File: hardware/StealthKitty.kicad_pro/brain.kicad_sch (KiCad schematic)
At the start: 16 parts, among them J4 M50-3600742, J5 Conn_ST_STDC14, SW1 SW_Push, SW2 SW_Push, U1 STM32G431CBUx, Y1 Crystal_GND24_Small

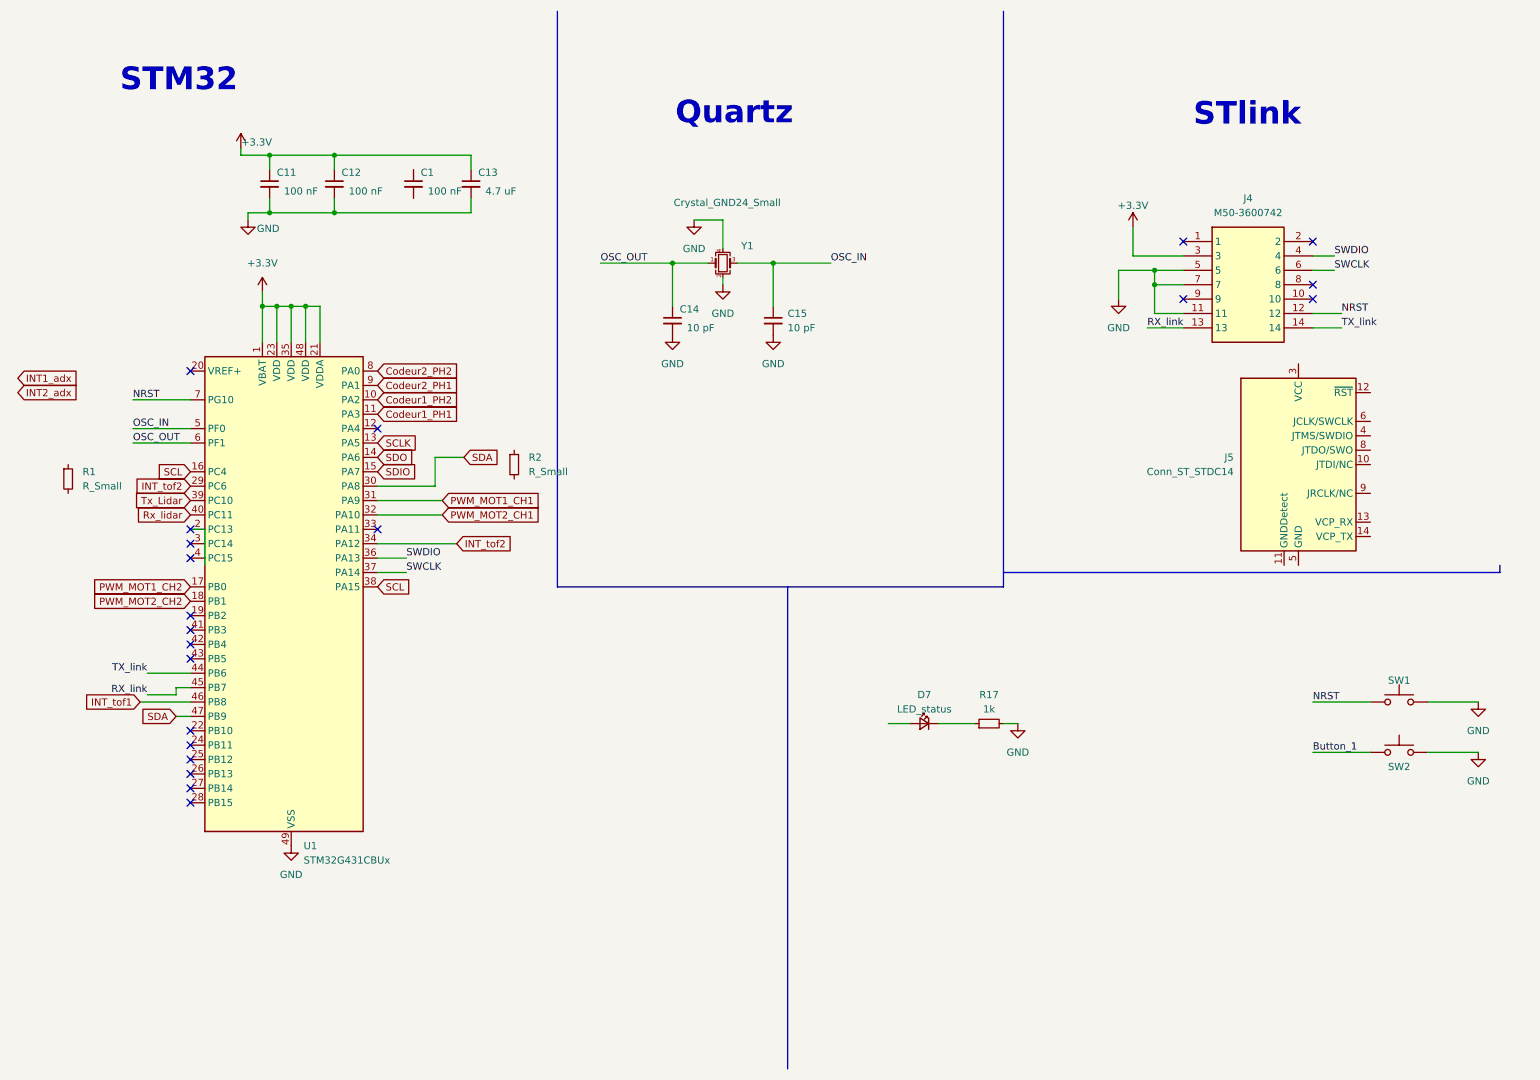
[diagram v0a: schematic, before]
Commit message: réassignation pins stm32, ajout des modifs de la partie power, ajout des modfis de la revue de projet 02/10/24, modifs du 3/10/24 voir readme
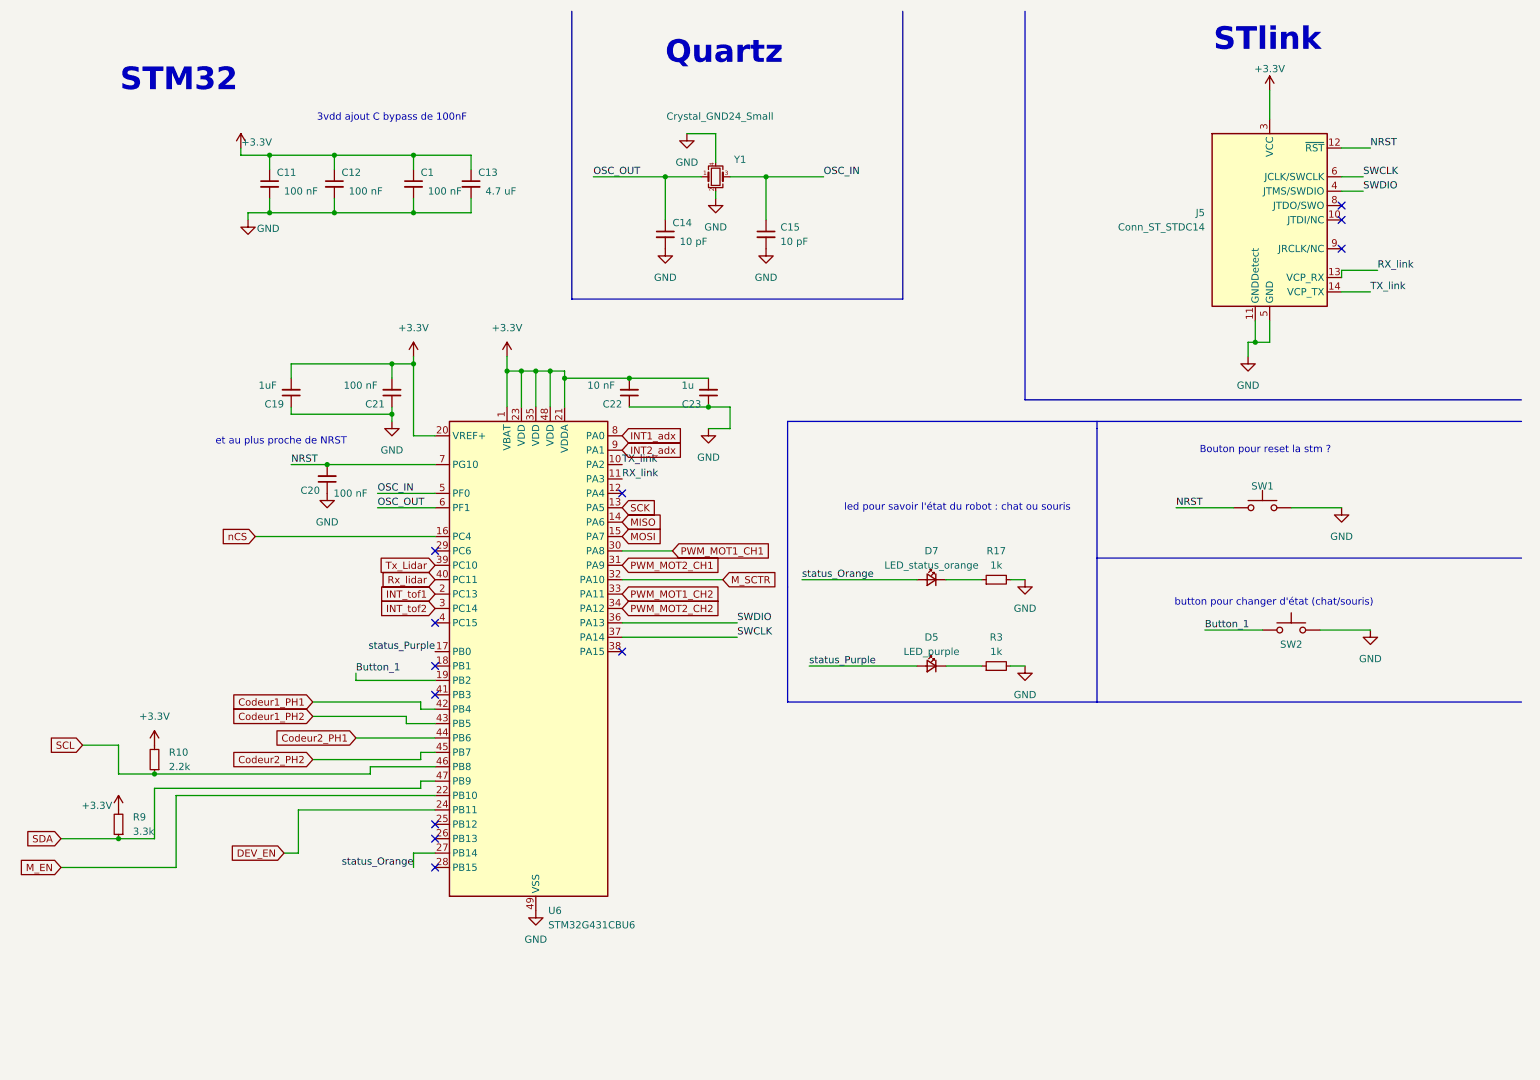
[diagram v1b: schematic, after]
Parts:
- removed J4: M50-3600742, Crystal:Crystal_SMD_3225-4Pin_3.2x2.5mm, symbol M50-3600742:M50-3600742
- removed R1, R2: R_Small, symbol Device:R_Small
- removed U1: STM32G431CBUx, Package_DFN_QFN:QFN-48-1EP_7x7mm_P0.5mm_EP5.6x5.6mm, symbol MCU_ST_STM32G4:STM32G431CBUx
- added C19: 1uF, symbol Device:C_Small
- added C20, C21: 100 nF, symbol Device:C_Small
- added C22: 10 nF, symbol Device:C_Small
- added C23: 1u, symbol Device:C_Small
- added D5: LED_purple, LED_SMD:LED_0603_1608Metric_Pad1.05x0.95mm_HandSolder, symbol Device:LED_Small
- added R10: 2.2k, symbol Device:R_Small
- added R3: 1k, Resistor_SMD:R_0603_1608Metric_Pad0.98x0.95mm_HandSolder, symbol Device:R_Small
- added R9: 3.3k, symbol Device:R_Small
- added U6: STM32G431CBU6, Package_DFN_QFN:QFN-48-1EP_7x7mm_P0.5mm_EP5.6x5.6mm, symbol MCU_ST_STM32G4:STM32G431CBUx
- D7: value LED_status -> LED_status_orange
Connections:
- net +3.3V: now also C1.1, J5.3 (VCC), C19.2, C21.2, C22.2, C23.2, R10.2, R9.2, U6.1 (VBAT), U6.20 (VREF+), U6.21 (VDDA), U6.23 (VDD), U6.35 (VDD), U6.48 (VDD)
- net Button_1: now also U6.19 (PB2)
- net Codeur1_PH1: now also U6.42 (PB4)
- net Codeur1_PH2: now also U6.43 (PB5)
- net Codeur2_PH1: now also U6.44 (PB6)
- net Codeur2_PH2: now also U6.45 (PB7)
- net GND: now also C1.2, J5.11 (GNDDetect), J5.5 (GND), J5.7 (GND), C19.1, C20.1, C21.1, C22.1, C23.1, R3.2, U6.49 (VSS)
- net INT1_adx: now also U6.8 (PA0)
- net INT2_adx: now also U6.9 (PA1)
- net INT_tof1: now also U6.2 (PC13)
- net INT_tof2: now also U6.3 (PC14)
- net NRST: now also J5.12 (~{RST}), C20.2, U6.7 (PG10)
- net OSC_IN: now also U6.5 (PF0)
- net OSC_OUT: now also U6.6 (PF1)
- net PWM_MOT1_CH1: now also U6.30 (PA8)
- net PWM_MOT1_CH2: now also U6.33 (PA11)
- net PWM_MOT2_CH1: now also U6.31 (PA9)
- net PWM_MOT2_CH2: now also U6.34 (PA12)
- net RX_link: now also J5.13 (VCP_RX), U6.11 (PA3)
- net Rx_lidar: now also U6.40 (PC11)
- net SCL: now also R10.1, U6.46 (PB8)
- net SDA: now also R9.1, U6.47 (PB9)
- net SWCLK: now also J5.6 (JCLK/SWCLK), U6.37 (PA14)
- net SWDIO: now also J5.4 (JTMS/SWDIO), U6.36 (PA13)
- net TX_link: now also J5.14 (VCP_TX), U6.10 (PA2)
- net Tx_Lidar: now also U6.39 (PC10)
- net status_Orange: now reaches D7.2 (A)
- net status_Orange: now also U6.27 (PB14)
- new net: D5.1 (K), R3.1
- new net DEV_EN: U6.24 (PB11)
- new net MISO: U6.14 (PA6)
- new net MOSI: U6.15 (PA7)
- new net M_EN: U6.22 (PB10)
- new net M_SCTR: U6.32 (PA10)
- new net SCK: U6.13 (PA5)
- new net nCS: U6.16 (PC4)
- new net status_Purple: D5.2 (A), U6.17 (PB0)
- no-connect marks 21 -> 12
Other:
- note added: "3vdd ajout C bypass de 100nF"
- note added: "Bouton pour reset la stm ?"
- note added: "button pour changer d'état (chat/souris)"
- note added: "et au plus proche de NRST"
- note added: "led pour savoir l'état du robot : chat ou souris"
- moved on the sheet: C14, C15, D7, J5, R17, SW1, SW2, Y1

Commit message: MAJ routage equipe
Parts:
- added H401, H402, H403, H404: ~, MountingHole:MountingHole_3.2mm_M3_Pad_Via, symbol Mechanical:MountingHole_Pad
- C1, C11, C12, C14, C15, C20, C21, C22: footprint (none) -> Capacitor_SMD:C_0402_1005Metric_Pad0.74x0.62mm_HandSolder
- C13, C19, C23: footprint (none) -> Capacitor_SMD:C_0603_1608Metric_Pad1.08x0.95mm_HandSolder
- R10, R9: footprint (none) -> Resistor_SMD:R_0603_1608Metric_Pad0.98x0.95mm_HandSolder
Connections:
- net GND: now also H401.1, H402.1, H403.1, H404.1

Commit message: Confirmation placement equipe
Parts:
- renumbered C11 to C401, C19 to C402, C20 to C403, C12 to C404, C21 to C405, C1 to C406, C13 to C407, C22 to C408, C14 to C409, C23 to C410, C15 to C411, D7 to D401, D5 to D402, J5 to J401, R9 to R401, R10 to R402, R17 to R403, R3 to R404, SW1 to SW401, SW2 to SW402, U6 to U401, Y1 to Y401

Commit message: Dernier Modif 08/10/2024
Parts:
- C401, C403, C404, C405, C406, C408, C409, C411: footprint Capacitor_SMD:C_0402_1005Metric_Pad0.74x0.62mm_HandSolder -> Capacitor_SMD:C_0402_1005Metric
- C402, C407, C410: footprint Capacitor_SMD:C_0603_1608Metric_Pad1.08x0.95mm_HandSolder -> Capacitor_SMD:C_0402_1005Metric
- R401, R402, R403, R404: footprint Resistor_SMD:R_0603_1608Metric_Pad0.98x0.95mm_HandSolder -> Resistor_SMD:R_0402_1005Metric
- SW401, SW402: footprint Button_Switch_SMD:SW_SPST_B3U-1000P -> Button_Switch_SMD:SW_Push_1P1T_NO_6x6mm_H9.5mm
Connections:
- net Button_1: now also U401.28 (PB15); no longer U401.19 (PB2)
- net INT1_adx: now also U401.19 (PB2); no longer U401.8 (PA0)
- net INT2_adx: now also U401.18 (PB1); no longer U401.9 (PA1)
- net status_Orange: now also U401.26 (PB13); no longer U401.27 (PB14)
- net status_Purple: now also U401.27 (PB14); no longer U401.17 (PB0)

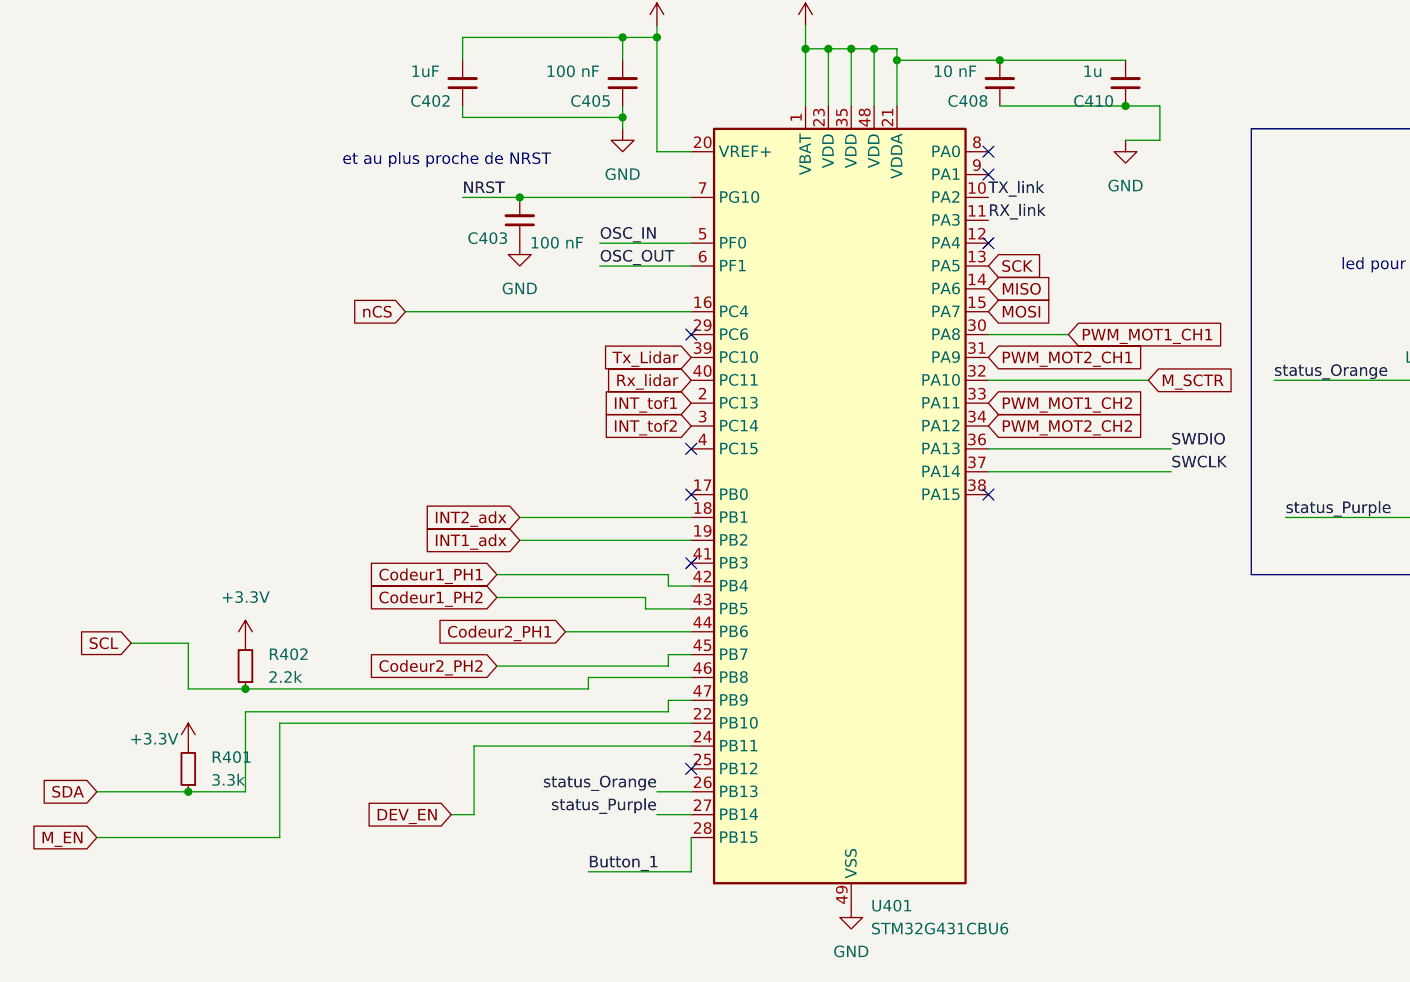
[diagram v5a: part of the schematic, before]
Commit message: MAJ première version routage
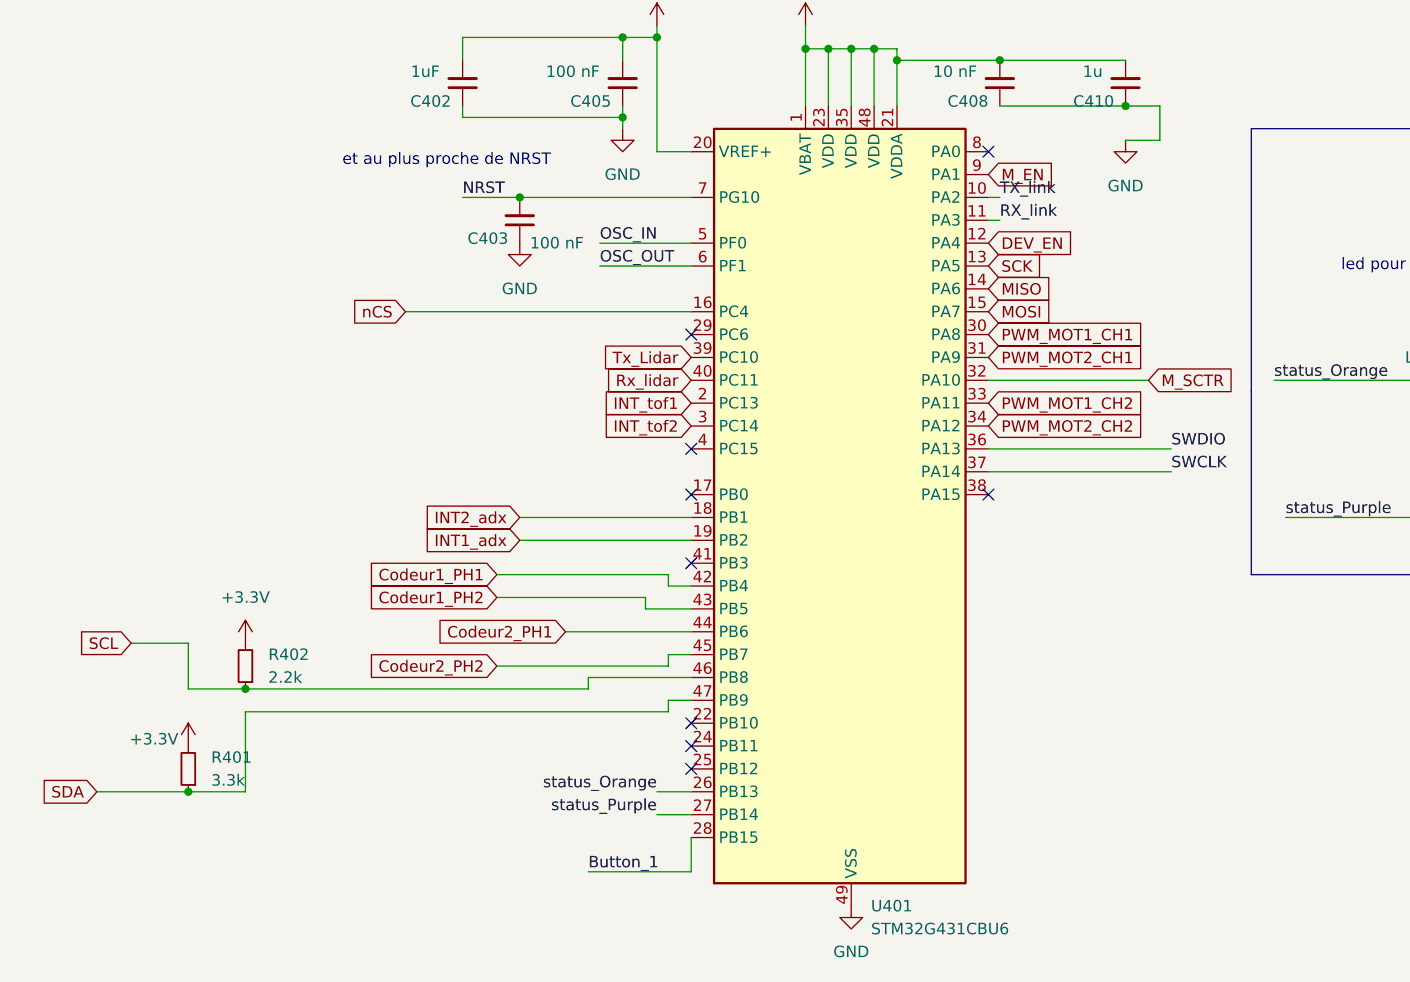
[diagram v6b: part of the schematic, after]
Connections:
- net DEV_EN: now also U401.12 (PA4); no longer U401.24 (PB11)
- net M_EN: now also U401.9 (PA1); no longer U401.22 (PB10)
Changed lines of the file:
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@@
-	)
-	(no_connect
-		(at 125.73 97.79)
 	)
 	(no_connect
@@
 	)
 	(no_connect
+		(at 92.71 151.13)
+	)
+	(no_connect
 		(at 125.73 125.73)
-	)
-	(no_connect
-		(at 125.73 90.17)
 	)
 	(no_connect
@@
 	)
 	(no_connect
+		(at 92.71 153.67)
+	)
+	(no_connect
 		(at 252.73 54.61)
 	)
@@
 	(wire
 		(pts
-			(xy 125.73 107.95) (xy 134.62 107.95)
-		)
-		(stroke
-			(width 0)
-			(type default)
-		)
-	)
-	(wire
-		(pts
 			(xy 142.24 34.29) (xy 142.24 39.37)
 		)
@@
 	(wire
 		(pts
+			(xy 127 95.25) (xy 125.73 95.25)
+		)
+		(stroke
+			(width 0)
+			(type default)
+		)
+	)
+	(wire
+		(pts
 			(xy 256.54 41.91) (xy 252.73 41.91)
 		)
@@
 	(wire
 		(pts
-			(xy 68.58 161.29) (xy 68.58 153.67)
-		)
-		(stroke
-			(width 0)
-			(type default)
-		)
-	)
-	(wire
-		(pts
 			(xy 236.22 71.12) (xy 236.22 73.66)
 		)
@@
 	(wire
 		(pts
-			(xy 46.99 151.13) (xy 92.71 151.13)
+			(xy 127 92.71) (xy 125.73 92.71)
 		)
 		(stroke
@@
 	(wire
 		(pts
-			(xy 46.99 163.83) (xy 46.99 151.13)
-		)
-		(stroke
-			(width 0)
-			(type default)
-		)
-	)
-	(wire
-		(pts
 			(xy 82.55 100.33) (xy 92.71 100.33)
 		)
@@
 	(wire
 		(pts
-			(xy 68.58 153.67) (xy 92.71 153.67)
-		)
-		(stroke
-			(width 0)
-			(type default)
-		)
-	)
-	(wire
-		(pts
 			(xy 236.22 71.12) (xy 237.49 71.12)
 		)
@@
 	(wire
 		(pts
-			(xy 26.67 163.83) (xy 46.99 163.83)
-		)
-		(stroke
-			(width 0)
-			(type default)
-		)
-	)
-	(wire
-		(pts
 			(xy 151.13 41.91) (xy 151.13 49.53)
 		)
@@
 		(pts
 			(xy 234.95 152.4) (xy 234.95 156.21)
-		)
-		(stroke
-			(width 0)
-			(type default)
-		)
-	)
-	(wire
-		(pts
-			(xy 66.04 161.29) (xy 68.58 161.29)
 		)
 		(stroke
@@
 	)
 	(label "TX_link"
-		(at 125.73 92.71 0)
+		(at 127 92.71 0)
 		(fields_autoplaced yes)
 		(effects
@@
 	)
 	(label "RX_link"
-		(at 125.73 95.25 0)
+		(at 127 95.25 0)
 		(fields_autoplaced yes)
 		(effects
@@
 	(global_label "PWM_MOT1_CH1"
 		(shape input)
-		(at 134.62 107.95 0)
+		(at 125.73 107.95 0)
 		(fields_autoplaced yes)
 		(effects
@@
 		)
 		(property "Intersheetrefs" "${INTERSHEET_REFS}"
-			(at 152.4822 107.95 0)
+			(at 143.5922 107.95 0)
 			(effects
 				(font
@@
 		)
 	)
+	(global_label "INT1_adx"
+		(shape input)
+		(at 73.66 130.81 180)
+		(fields_autoplaced yes)
+		(effects
+			(font
+				(size 1.27 1.27)
+			)
+			(justify right)
+		)
+		(property "Intersheetrefs" "${INTERSHEET_REFS}"
+			(at 62.2687 130.81 0)
+			(effects
+				(font
+					(size 1.27 1.27)
+				)
+				(justify right)
+				(hide yes)
+			)
+		)
+	)
+	(global_label "DEV_EN"
+		(shape input)
+		(at 125.73 97.79 0)
+		(fields_autoplaced yes)
+		(effects
+			(font
+				(size 1.27 1.27)
+			)
+			(justify left)
+		)
+		(property "Intersheetrefs" "${INTERSHEET_REFS}"
+			(at 135.6699 97.79 0)
+			(effects
+				(font
+					(size 1.27 1.27)
+				)
+				(justify left)
+				(hide yes)
+			)
+		)
+	)
 	(global_label "M_EN"
 		(shape input)
-		(at 26.67 163.83 180)
-		(fields_autoplaced yes)
-		(effects
-			(font
-				(size 1.27 1.27)
-			)
-			(justify right)
-		)
-		(property "Intersheetrefs" "${INTERSHEET_REFS}"
-			(at 18.7863 163.83 0)
-			(effects
-				(font
-					(size 1.27 1.27)
-				)
-				(justify right)
-				(hide yes)
-			)
-		)
-	)
-	(global_label "INT1_adx"
-		(shape input)
-		(at 73.66 130.81 180)
-		(fields_autoplaced yes)
-		(effects
-			(font
-				(size 1.27 1.27)
-			)
-			(justify right)
-		)
-		(property "Intersheetrefs" "${INTERSHEET_REFS}"
-			(at 62.2687 130.81 0)
-			(effects
-				(font
-					(size 1.27 1.27)
-				)
-				(justify right)
-				(hide yes)
-			)
-		)
-	)
-	(global_label "DEV_EN"
-		(shape input)
-		(at 66.04 161.29 180)
-		(fields_autoplaced yes)
-		(effects
-			(font
-				(size 1.27 1.27)
-			)
-			(justify right)
-		)
-		(property "Intersheetrefs" "${INTERSHEET_REFS}"
-			(at 56.1001 161.29 0)
-			(effects
-				(font
-					(size 1.27 1.27)
-				)
-				(justify right)
-				(hide yes)
-			)
+		(at 125.73 90.17 0)
+		(fields_autoplaced yes)
+		(effects
+			(font
+				(size 1.27 1.27)
+			)
+			(justify left)
+		)
+		(property "Intersheetrefs" "${INTERSHEET_REFS}"
+			(at 133.6137 90.17 0)
+			(effects
+				(font
+					(size 1.27 1.27)
+				)
+				(justify left)
+				(hide yes)
+			)

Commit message: Modif PCB 16/10/2024  V1
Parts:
- added D403: LED_status_LiDAR, LED_SMD:LED_0603_1608Metric_Pad1.05x0.95mm_HandSolder, symbol Device:LED_Small
- added R405: 1k, Resistor_SMD:R_0402_1005Metric, symbol Device:R_Small
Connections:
- net GND: now also R405.2
- new net: D403.1 (K), R405.1
- new net status_LiDar: D403.2 (A)
- no-connect marks 12 -> 11
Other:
- moved on the sheet: D401, D402, H401, H402, H403, H404, R403, R404
